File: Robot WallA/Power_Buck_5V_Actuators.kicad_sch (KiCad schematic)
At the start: 18 parts, among them J14 NID35-5, Q1 BSS138

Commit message: Continue to route
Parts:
- C57: footprint Capacitor_SMD:C_0805_2012Metric_Pad1.18x1.45mm_HandSolder -> SamacSys_Parts:EEE1AA220WR; Height (none) -> 5.5; Manufacturer_Part_Number (none) -> EEE-FN1E220R
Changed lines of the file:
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@@
+	)
+	(junction
+		(at 210.82 55.88)
+		(diameter 0)
+		(color 0 0 0 0)
+	)
+	(junction
+		(at 210.82 48.26)
+		(diameter 0)
+		(color 0 0 0 0)
 	)
 	(junction
@@
 	)
 	(junction
-		(at 209.55 55.88)
-		(diameter 0)
-		(color 0 0 0 0)
-	)
-	(junction
 		(at 138.43 80.01)
 		(diameter 0)
@@
 	)
 	(junction
-		(at 209.55 48.26)
-		(diameter 0)
-		(color 0 0 0 0)
-	)
-	(junction
 		(at 233.68 48.26)
 		(diameter 0)
@@
 	(wire
 		(pts
-			(xy 200.66 48.26) (xy 209.55 48.26)
+			(xy 200.66 48.26) (xy 210.82 48.26)
 		)
 		(stroke
@@
 	(wire
 		(pts
+			(xy 210.82 48.26) (xy 223.52 48.26)
+		)
+		(stroke
+			(width 0)
+			(type default)
+		)
+	)
+	(wire
+		(pts
+			(xy 210.82 55.88) (xy 223.52 55.88)
+		)
+		(stroke
+			(width 0)
+			(type default)
+		)
+	)
+	(wire
+		(pts
 			(xy 223.52 109.22) (xy 223.52 111.76)
 		)
@@
 	(wire
 		(pts
-			(xy 200.66 55.88) (xy 209.55 55.88)
-		)
-		(stroke
-			(width 0)
-			(type default)
-		)
-	)
-	(wire
-		(pts
 			(xy 87.63 54.61) (xy 97.79 54.61)
 		)
@@
 	(wire
 		(pts
-			(xy 209.55 55.88) (xy 223.52 55.88)
+			(xy 200.66 55.88) (xy 210.82 55.88)
 		)
 		(stroke
@@
 		(pts
 			(xy 138.43 80.01) (xy 138.43 82.55)
-		)
-		(stroke
-			(width 0)
-			(type default)
-		)
-	)
-	(wire
-		(pts
-			(xy 209.55 48.26) (xy 223.52 48.26)
 		)
 		(stroke
@@
 				(path "/117fd49e-499d-4b54-b58c-f6b538ecca4a/d5f4dab0-e2de-4083-971d-4b1eb9c8d4bb/1e067d8d-e8a8-481d-ab40-c8016ce22eb0"
 					(reference "#FLG05")
-					(unit 1)
-				)
-			)
-		)
-	)
-	(symbol
-		(lib_id "Device:C_Polarized")
-		(at 209.55 52.07 0)
-		(unit 1)
-		(exclude_from_sim no)
-		(in_bom yes)
-		(on_board yes)
-		(dnp no)
-		(property "Reference" "C57"
-			(at 202.946 52.07 0)
-			(effects
-				(font
-					(size 1.27 1.27)
-				)
-				(justify left)
-			)
-		)
-		(property "Value" "22uF/25V"
-			(at 204.978 55.118 0)
-			(effects
-				(font
-					(size 1.27 1.27)
-				)
-				(justify left)
-			)
-		)
-		(property "Footprint" "Capacitor_SMD:C_0805_2012Metric_Pad1.18x1.45mm_HandSolder"
-			(at 210.5152 55.88 0)
-			(effects
-				(font
-					(size 1.27 1.27)
-				)
-				(hide yes)
-			)
-		)
-		(property "Datasheet" "~"
-			(at 209.55 52.07 0)
-			(effects
-				(font
-					(size 1.27 1.27)
-				)
-				(hide yes)
-			)
-		)
-		(property "Description" "Polarized capacitor"
-			(at 209.55 52.07 0)
-			(effects
-				(font
-					(size 1.27 1.27)
-				)
-				(hide yes)
-			)
-		)
-		(pin "1"
-		)
-		(pin "2"
-		)
-		(instances
-			(project "PCB"
-				(path "/117fd49e-499d-4b54-b58c-f6b538ecca4a/d5f4dab0-e2de-4083-971d-4b1eb9c8d4bb/1e067d8d-e8a8-481d-ab40-c8016ce22eb0"
-					(reference "C57")
 					(unit 1)
 				)
@@
 					(unit 1)
 				)
+			)
+		)
+	)
+	(symbol
+		(lib_id "Device:C_Polarized")
+		(at 210.82 52.07 0)
+		(unit 1)
+		(exclude_from_sim no)
+		(in_bom yes)
+		(on_board yes)
+		(dnp no)
+		(property "Reference" "C57"
+			(at 204.216 52.07 0)
+			(effects
+				(font
+					(size 1.27 1.27)
+				)
+				(justify left)
+			)
+		)
+		(property "Value" "22uF/25V"
+			(at 206.248 55.118 0)
+			(effects
+				(font
+					(size 1.27 1.27)
+				)
+				(justify left)
+			)
+		)
+		(property "Footprint" "SamacSys_Parts:EEE1AA220WR"
+			(at 211.7852 55.88 0)
+			(effects
+				(font
+					(size 1.27 1.27)
+				)
+				(hide yes)
+			)
+		)
+		(property "Datasheet" "~"
+			(at 210.82 52.07 0)
+			(effects
+				(font
+					(size 1.27 1.27)
+				)
+				(hide yes)
+			)
+		)
+		(property "Description" "Polarized capacitor"
+			(at 210.82 52.07 0)
+			(effects
+				(font
+					(size 1.27 1.27)
+				)
+				(hide yes)
+			)
+		)
+		(property "Height" "5.5"
+			(at 210.82 52.07 0)
+			(effects
+				(font
+					(size 1.27 1.27)
+				)
+				(hide yes)
+			)
+		)
+		(property "Manufacturer_Part_Number" "EEE-FN1E220R"
+			(at 210.82 52.07 0)
+			(effects
+				(font
+					(size 1.27 1.27)
+				)
+				(hide yes)
+			)
+		)
+		(pin "1"
+		)
+		(pin "2"
+		)
+		(instances
+			(project "Robot WallA"
+				(path "/117fd49e-499d-4b54-b58c-f6b538ecca4a/d5f4dab0-e2de-4083-971d-4b1eb9c8d4bb/1e067d8d-e8a8-481d-ab40-c8016ce22eb0"
+					(reference "C57")
+					(unit 1)
+				)

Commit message: Reworked 12V and 5V power supplies, continue routing
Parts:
- removed C51: 120uF/25V, SamacSys_Parts:EEE0JA331XP, symbol Device:C_Polarized
- removed C52, C53, C54: 47nF/25V, Capacitor_SMD:C_0603_1608Metric_Pad1.08x0.95mm_HandSolder, symbol Device:C
- removed C55, C56: 4.7uF/25V, Capacitor_SMD:C_1210_3225Metric_Pad1.33x2.70mm_HandSolder, symbol Device:C
- removed C57: 22uF/25V, SamacSys_Parts:EEE1AA220WR, symbol Device:C_Polarized
- removed C58, C59, C60: 4.7uF/50V, Capacitor_SMD:C_0805_2012Metric_Pad1.18x1.45mm_HandSolder, symbol Device:C
- removed C61: 10nF/50V, Capacitor_SMD:C_0805_2012Metric_Pad1.18x1.45mm_HandSolder, symbol Device:C
- removed J14: NID35-5, SamacSys_Parts:NID355, symbol SamacSys_Parts:NID35-5
- removed Q1: BSS138, Package_TO_SOT_SMD:SOT-23, symbol Transistor_FET:BSS138
- removed R31: 100k, Resistor_SMD:R_0603_1608Metric_Pad0.98x0.95mm_HandSolder, symbol Device:R
- removed R32: 10k, Resistor_SMD:R_0603_1608Metric_Pad0.98x0.95mm_HandSolder, symbol Device:R
- removed RV2: Trim 10k, SamacSys_Parts:TC33X2503E, symbol Device:R_Potentiometer_Trim
- added C118, C87: 4.7uF/50V, Capacitor_SMD:C_1210_3225Metric_Pad1.33x2.70mm_HandSolder, symbol Device:C
- added C119: 10nF/50V, Capacitor_SMD:C_0805_2012Metric_Pad1.18x1.45mm_HandSolder, symbol Device:C
- added C120: 2.2uF/50V, Capacitor_SMD:C_1210_3225Metric_Pad1.33x2.70mm_HandSolder, symbol Device:C
- added C121, C122, C123: 47nF/25V, Capacitor_SMD:C_0603_1608Metric_Pad1.08x0.95mm_HandSolder, symbol Device:C
- added C124, C125: 4.7uF/25V, Capacitor_SMD:C_1210_3225Metric_Pad1.33x2.70mm_HandSolder, symbol Device:C
- added C86: 330uF, SamacSys_Parts:CAPPRD500W65D1000H1800, symbol Device:C_Polarized
- added JP12: Closed, Jumper:SolderJumper-2_P1.3mm_Bridged_RoundedPad1.0x1.5mm, symbol Jumper:Jumper_2_Bridged
- added JP13: Open, Jumper:SolderJumper-2_P1.3mm_Open_RoundedPad1.0x1.5mm, symbol Jumper:Jumper_2_Open
- added Q6: BSS138, Package_TO_SOT_SMD:SOT-23, symbol Transistor_FET:BSS138
- added R54: 21k, Resistor_SMD:R_0603_1608Metric_Pad0.98x0.95mm_HandSolder, symbol Device:R
- added R60: 10k, Resistor_SMD:R_0603_1608Metric_Pad0.98x0.95mm_HandSolder, symbol Device:R
- added RV3: Trim 2k, SamacSys_Parts:TC42X2202E, symbol Device:R_Potentiometer_Trim
- added U9: PTN78060W_EUW-7, Module:Texas_EUW_R-PDSS-T7_THT, symbol Converter_DCDC:PTN78060W_EUW-7
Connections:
- net GND: now also C118.2, C119.2, C120.2, C121.2, C122.2, C123.2, C124.2, C125.2, C86.2, C87.2, JP12.1 (A), Q6.2 (S), R60.2, RV3.2, U9.1 (GND), U9.7 (GND)
- net GPIO_ENABLE_5V: now also Q6.1 (G), R60.1
- net IN: now also C120.1, C121.1, C122.1, C123.1, C124.1, C125.1, U9.2 (VI)
- net OUT: now also C118.1, C119.1, C86.1, C87.1, U9.5 (VO_Sense), U9.6 (VO)
- new net: Q6.3 (D), U9.3 (~{Inhibit})
- new net: JP12.2 (B), JP13.1 (A), R54.2
- new net: JP13.2 (B), RV3.1
- new net TRIM: R54.1, U9.4 (VO_Adj)
- no-connect marks 0 -> 1
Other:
- note removed: "Si Vin=16V et Vout 5V --> Rendement >93% Avec un courant de 3A théorique (PC calcul) --> Puissance à dissiper de 1,05W Ne doit pas dépasser 55°C D'après la doc il ne faut pas forcément de radiateur, juste un ventilo Mettre un capteur de température pour monitorer?"
- note removed: "footprint size 10n --> 0805 47n --> 0603 4,7uF --> 1210"
- moved on the sheet: D5, R30

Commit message: Correct a lot of error in DRC
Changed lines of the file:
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@@
-	)
-	(junction
-		(at 261.62 29.21)
-		(diameter 0)
-		(color 0 0 0 0)
 	)
 	(junction
@@
 	(wire
 		(pts
-			(xy 257.81 29.21) (xy 261.62 29.21)
-		)
-		(stroke
-			(width 0)
-			(type default)
-		)
-	)
-	(wire
-		(pts
 			(xy 154.94 96.52) (xy 153.67 96.52)
 		)
@@
 	(wire
 		(pts
-			(xy 261.62 29.21) (xy 264.16 29.21)
+			(xy 257.81 29.21) (xy 264.16 29.21)
 		)
 		(stroke
@@
 	)
 	(symbol
+		(lib_id "power:PWR_FLAG")
+		(at 43.18 46.99 0)
+		(unit 1)
+		(exclude_from_sim no)
+		(in_bom yes)
+		(on_board yes)
+		(dnp no)
+		(fields_autoplaced yes)
+		(property "Reference" "#FLG07"
+			(at 43.18 45.085 0)
+			(effects
+				(font
+					(size 1.27 1.27)
+				)
+				(hide yes)
+			)
+		)
+		(property "Value" "PWR_FLAG"
+			(at 43.18 41.91 0)
+			(effects
+				(font
+					(size 1.27 1.27)
+				)
+				(hide yes)
+			)
+		)
+		(property "Footprint" ""
+			(at 43.18 46.99 0)
+			(effects
+				(font
+					(size 1.27 1.27)
+				)
+				(hide yes)
+			)
+		)
+		(property "Datasheet" "~"
+			(at 43.18 46.99 0)
+			(effects
+				(font
+					(size 1.27 1.27)
+				)
+				(hide yes)
+			)
+		)
+		(property "Description" "Special symbol for telling ERC where power comes from"
+			(at 43.18 46.99 0)
+			(effects
+				(font
+					(size 1.27 1.27)
+				)
+				(hide yes)
+			)
+		)
+		(pin "1"
+		)
+		(instances
+			(project "Robot WallA"
+				(path "/117fd49e-499d-4b54-b58c-f6b538ecca4a/d5f4dab0-e2de-4083-971d-4b1eb9c8d4bb/1e067d8d-e8a8-481d-ab40-c8016ce22eb0"
+					(reference "#FLG07")
+					(unit 1)
+				)
+			)
+		)
+	)
+	(symbol
 		(lib_id "Jumper:Jumper_2_Open")
 		(at 248.92 115.57 90)
@@
 					(unit 1)
 				)
-			)
-		)
-	)
-	(symbol
-		(lib_id "power:PWR_FLAG")
-		(at 261.62 29.21 0)
-		(unit 1)
-		(exclude_from_sim no)
-		(in_bom yes)
-		(on_board yes)
-		(dnp no)
-		(fields_autoplaced yes)
-		(property "Reference" "#FLG05"
-			(at 261.62 27.305 0)
-			(effects
-				(font
-					(size 1.27 1.27)
-				)
-				(hide yes)
-			)
-		)
-		(property "Value" "PWR_FLAG"
-			(at 261.62 24.13 0)
-			(effects
-				(font
-					(size 1.27 1.27)
-				)
-				(hide yes)
-			)
-		)
-		(property "Footprint" ""
-			(at 261.62 29.21 0)
-			(effects
-				(font
-					(size 1.27 1.27)
-				)
-				(hide yes)
-			)
-		)
-		(property "Datasheet" "~"
-			(at 261.62 29.21 0)
-			(effects
-				(font
-					(size 1.27 1.27)
-				)
-				(hide yes)
-			)
-		)
-		(property "Description" "Special symbol for telling ERC where power comes from"
-			(at 261.62 29.21 0)
-			(effects
-				(font
-					(size 1.27 1.27)
-				)
-				(hide yes)
-			)
-		)
-		(pin "1"
-		)
-		(instances
-			(project "Robot WallA"
-				(path "/117fd49e-499d-4b54-b58c-f6b538ecca4a/d5f4dab0-e2de-4083-971d-4b1eb9c8d4bb/1e067d8d-e8a8-481d-ab40-c8016ce22eb0"
-					(reference "#FLG05")
-					(unit 1)
-				)

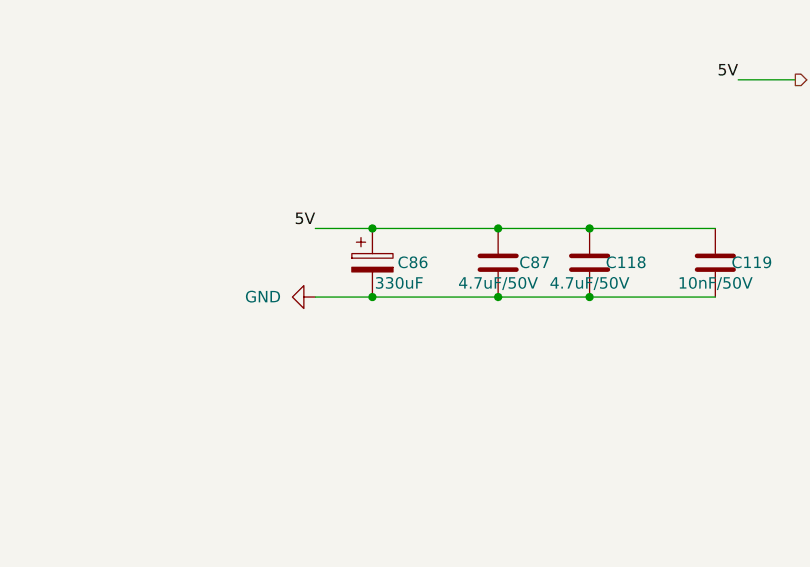
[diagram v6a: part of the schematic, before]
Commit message: Corrected all DRC erros, added info on PCB
modified distance meter connectors to be horizontal
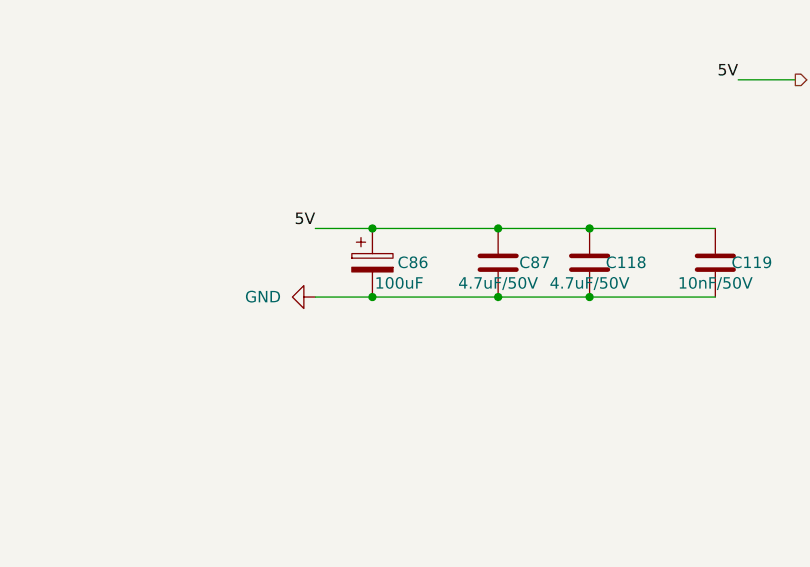
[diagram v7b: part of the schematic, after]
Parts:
- C86: value 330uF -> 100uF; footprint SamacSys_Parts:CAPPRD500W65D1000H1800 -> SamacSys_Parts:CAPPRD350W65D800H1250; Manufacturer_Part_Number EEU-FC1V331 -> (none)
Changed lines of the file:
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@@
+	)
+	(junction
+		(at 231.14 45.72)
+		(diameter 0)
+		(color 0 0 0 0)
+	)
+	(junction
+		(at 217.17 53.34)
+		(diameter 0)
+		(color 0 0 0 0)
+	)
+	(junction
+		(at 154.94 97.79)
+		(diameter 0)
+		(color 0 0 0 0)
+	)
+	(junction
+		(at 118.11 113.03)
+		(diameter 0)
+		(color 0 0 0 0)
+	)
+	(junction
+		(at 64.77 54.61)
+		(diameter 0)
+		(color 0 0 0 0)
+	)
+	(junction
+		(at 55.88 54.61)
+		(diameter 0)
+		(color 0 0 0 0)
+	)
+	(junction
+		(at 243.84 110.49)
+		(diameter 0)
+		(color 0 0 0 0)
+	)
+	(junction
+		(at 43.18 54.61)
+		(diameter 0)
+		(color 0 0 0 0)
+	)
+	(junction
+		(at 87.63 46.99)
+		(diameter 0)
+		(color 0 0 0 0)
+	)
+	(junction
+		(at 241.3 53.34)
+		(diameter 0)
+		(color 0 0 0 0)
+	)
+	(junction
+		(at 241.3 45.72)
+		(diameter 0)
+		(color 0 0 0 0)
+	)
+	(junction
+		(at 107.95 104.14)
+		(diameter 0)
+		(color 0 0 0 0)
+	)
+	(junction
+		(at 73.66 46.99)
+		(diameter 0)
+		(color 0 0 0 0)
+	)
+	(junction
+		(at 73.66 54.61)
+		(diameter 0)
+		(color 0 0 0 0)
+	)
+	(junction
+		(at 55.88 46.99)
+		(diameter 0)
+		(color 0 0 0 0)
+	)
+	(junction
+		(at 231.14 53.34)
+		(diameter 0)
+		(color 0 0 0 0)
+	)
+	(junction
+		(at 64.77 46.99)
+		(diameter 0)
+		(color 0 0 0 0)
 	)
 	(junction
@@
 	)
 	(junction
-		(at 231.14 45.72)
-		(diameter 0)
-		(color 0 0 0 0)
-	)
-	(junction
-		(at 154.94 97.79)
-		(diameter 0)
-		(color 0 0 0 0)
-	)
-	(junction
-		(at 118.11 113.03)
-		(diameter 0)
-		(color 0 0 0 0)
-	)
-	(junction
-		(at 64.77 54.61)
-		(diameter 0)
-		(color 0 0 0 0)
-	)
-	(junction
-		(at 55.88 54.61)
-		(diameter 0)
-		(color 0 0 0 0)
-	)
-	(junction
-		(at 243.84 110.49)
-		(diameter 0)
-		(color 0 0 0 0)
-	)
-	(junction
-		(at 43.18 54.61)
-		(diameter 0)
-		(color 0 0 0 0)
-	)
-	(junction
-		(at 87.63 46.99)
-		(diameter 0)
-		(color 0 0 0 0)
-	)
-	(junction
-		(at 241.3 53.34)
-		(diameter 0)
-		(color 0 0 0 0)
-	)
-	(junction
-		(at 241.3 45.72)
-		(diameter 0)
-		(color 0 0 0 0)
-	)
-	(junction
-		(at 107.95 104.14)
-		(diameter 0)
-		(color 0 0 0 0)
-	)
-	(junction
-		(at 73.66 46.99)
-		(diameter 0)
-		(color 0 0 0 0)
-	)
-	(junction
-		(at 217.17 53.34)
-		(diameter 0)
-		(color 0 0 0 0)
-	)
-	(junction
-		(at 73.66 54.61)
-		(diameter 0)
-		(color 0 0 0 0)
-	)
-	(junction
-		(at 55.88 46.99)
-		(diameter 0)
-		(color 0 0 0 0)
-	)
-	(junction
-		(at 231.14 53.34)
-		(diameter 0)
-		(color 0 0 0 0)
-	)
-	(junction
-		(at 64.77 46.99)
-		(diameter 0)
-		(color 0 0 0 0)
-	)
-	(junction
 		(at 87.63 54.61)
 		(diameter 0)
@@
 	(wire
 		(pts
+			(xy 210.82 45.72) (xy 217.17 45.72)
+		)
+		(stroke
+			(width 0)
+			(type default)
+		)
+	)
+	(wire
+		(pts
+			(xy 241.3 45.72) (xy 255.27 45.72)
+		)
+		(stroke
+			(width 0)
+			(type default)
+		)
+	)
+	(wire
+		(pts
 			(xy 217.17 45.72) (xy 231.14 45.72)
 		)
@@
 	(wire
 		(pts
-			(xy 241.3 45.72) (xy 255.27 45.72)
-		)
-		(stroke
-			(width 0)
-			(type default)
-		)
-	)
-	(wire
-		(pts
-			(xy 210.82 45.72) (xy 217.17 45.72)
-		)
-		(stroke
-			(width 0)
-			(type default)
-		)
-	)
-	(wire
-		(pts
 			(xy 55.88 54.61) (xy 64.77 54.61)
 		)
@@
 	(wire
 		(pts
+			(xy 217.17 53.34) (xy 231.14 53.34)
+		)
+		(stroke
+			(width 0)
+			(type default)
+		)
+	)
+	(wire
+		(pts
 			(xy 43.18 54.61) (xy 55.88 54.61)
 		)
@@
 		(pts
 			(xy 87.63 54.61) (xy 97.79 54.61)
-		)
-		(stroke
-			(width 0)
-			(type default)
-		)
-	)
-	(wire
-		(pts
-			(xy 217.17 53.34) (xy 231.14 53.34)
 		)
 		(stroke
@@
 	)
 	(symbol
+		(lib_id "Device:C_Polarized")
+		(at 217.17 49.53 0)
+		(unit 1)
+		(exclude_from_sim no)
+		(in_bom yes)
+		(on_board yes)
+		(dnp no)
+		(property "Reference" "C86"
+			(at 219.964 49.53 0)
+			(effects
+				(font
+					(size 1.27 1.27)
+				)
+				(justify left)
+			)
+		)
+		(property "Value" "100uF"
+			(at 217.424 51.816 0)
+			(effects
+				(font
+					(size 1.27 1.27)
+				)
+				(justify left)
+			)
+		)
+		(property "Footprint" "SamacSys_Parts:CAPPRD350W65D800H1250"
+			(at 218.1352 53.34 0)
+			(effects
+				(font
+					(size 1.27 1.27)
+				)
+				(hide yes)
+			)
+		)
+		(property "Datasheet" "~"
+			(at 217.17 49.53 0)
+			(effects
+				(font
+					(size 1.27 1.27)
+				)
+				(hide yes)
+			)
+		)
+		(property "Description" "Polarized capacitor"
+			(at 217.17 49.53 0)
+			(effects
+				(font
+					(size 1.27 1.27)
+				)
+				(hide yes)
+			)
+		)
+		(property "Manufacturer_Part_Number" ""
+			(at 217.17 49.53 0)
+			(effects
+				(font
+					(size 1.27 1.27)
+				)
+				(hide yes)
+			)
+		)
+		(pin "1"
+		)
+		(pin "2"
+		)
+		(instances
+			(project "Robot WallA"
+				(path "/117fd49e-499d-4b54-b58c-f6b538ecca4a/d5f4dab0-e2de-4083-971d-4b1eb9c8d4bb/1e067d8d-e8a8-481d-ab40-c8016ce22eb0"
+					(reference "C86")
+					(unit 1)
+				)
+			)
+		)
+	)
+	(symbol
 		(lib_id "Device:C")
 		(at 231.14 49.53 0)
@@
 					(unit 1)
 				)
-			)
-		)
-	)
-	(symbol
-		(lib_id "Device:C_Polarized")
-		(at 217.17 49.53 0)
-		(unit 1)
-		(exclude_from_sim no)
-		(in_bom yes)
-		(on_board yes)
-		(dnp no)
-		(property "Reference" "C86"
-			(at 219.964 49.53 0)
-			(effects
-				(font
-					(size 1.27 1.27)
-				)
-				(justify left)
-			)
-		)
-		(property "Value" "330uF"
-			(at 217.424 51.816 0)
-			(effects
-				(font
-					(size 1.27 1.27)
-				)
-				(justify left)
-			)
-		)
-		(property "Footprint" "SamacSys_Parts:CAPPRD500W65D1000H1800"
-			(at 218.1352 53.34 0)
-			(effects
-				(font
-					(size 1.27 1.27)
-				)
-				(hide yes)
-			)
-		)
-		(property "Datasheet" "~"
-			(at 217.17 49.53 0)
-			(effects
-				(font
-					(size 1.27 1.27)
-				)
-				(hide yes)
-			)
-		)
-		(property "Description" "Polarized capacitor"
-			(at 217.17 49.53 0)
-			(effects
-				(font
-					(size 1.27 1.27)
-				)
-				(hide yes)
-			)
-		)
-		(property "Manufacturer_Part_Number" "EEU-FC1V331"
-			(at 217.17 49.53 0)
-			(effects
-				(font
-					(size 1.27 1.27)
-				)
-				(hide yes)
-			)
-		)
-		(pin "1"
-		)
-		(pin "2"
-		)
-		(instances
-			(project "Robot WallA"
-				(path "/117fd49e-499d-4b54-b58c-f6b538ecca4a/d5f4dab0-e2de-4083-971d-4b1eb9c8d4bb/1e067d8d-e8a8-481d-ab40-c8016ce22eb0"
-					(reference "C86")
-					(unit 1)
-				)

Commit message: Updated fab files.
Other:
- company: (none) -> Socotec Monitoring
- title: (none) -> Robot Wall-A
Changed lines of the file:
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@@
 	(generator_version "9.0")
 	(paper "A4")
+	(title_block
+		(title "Robot Wall-A")
+		(date "2025-09-20")
+		(rev "v1.0")
+		(company "Socotec Monitoring")
+		(comment 1 "GDU")
+		(comment 2 "THO")
+	)
 	(junction
 		(at 43.18 46.99)
@@
 			)
 		)
+		(property "MPN" ""
+			(at 55.88 50.8 0)
+			(effects
+				(font
+					(size 1.27 1.27)
+				)
+				(hide yes)
+			)
+		)
 		(pin "1"
 		)
@@
 			)
 		)
+		(property "MPN" ""
+			(at 115.57 104.14 0)
+			(effects
+				(font
+					(size 1.27 1.27)
+				)
+				(hide yes)
+			)
+		)
 		(pin "2"
 		)
@@
 			)
 		)
+		(property "MPN" ""
+			(at 87.63 50.8 0)
+			(effects
+				(font
+					(size 1.27 1.27)
+				)
+				(hide yes)
+			)
+		)
 		(pin "1"
 		)
@@
 			)
 		)
+		(property "MPN" ""
+			(at 107.95 109.22 90)
+			(effects
+				(font
+					(size 1.27 1.27)
+				)
+				(hide yes)
+			)
+		)
 		(pin "1"
 		)
@@
 			)
 		)
+		(property "MPN" ""
+			(at 248.92 115.57 90)
+			(effects
+				(font
+					(size 1.27 1.27)
+				)
+				(hide yes)
+			)
+		)
 		(pin "1"
 		)
@@
 			)
 		)
+		(property "MPN" ""
+			(at 64.77 50.8 0)
+			(effects
+				(font
+					(size 1.27 1.27)
+				)
+				(hide yes)
+			)
+		)
 		(pin "1"
 		)
@@
 			)
 		)
+		(property "MPN" ""
+			(at 157.48 50.8 90)
+			(effects
+				(font
+					(size 1.27 1.27)
+				)
+				(hide yes)
+			)
+		)
 		(pin "1"
 		)
@@
 			)
 		)
+		(property "MPN" ""
+			(at 238.76 115.57 90)
+			(effects
+				(font
+					(size 1.27 1.27)
+				)
+				(hide yes)
+			)
+		)
 		(pin "2"
 		)
@@
 			)
 		)
+		(property "MPN" ""
+			(at 255.27 49.53 0)
+			(effects
+				(font
+					(size 1.27 1.27)
+				)
+				(hide yes)
+			)
+		)
 		(pin "1"
 		)
@@
 			)
 		)
+		(property "MPN" ""
+			(at 248.92 124.46 0)
+			(effects
+				(font
+					(size 1.27 1.27)
+				)
+				(hide yes)
+			)
+		)
 		(pin "2"
 		)
@@
 			)
 		)
+		(property "MPN" ""
+			(at 97.79 50.8 0)
+			(effects
+				(font
+					(size 1.27 1.27)
+				)
+				(hide yes)
+			)
+		)
 		(pin "1"
 		)
@@
 			)
 		)
+		(property "MPN" ""
+			(at 140.97 99.06 0)
+			(effects
+				(font
+					(size 1.27 1.27)
+				)
+				(hide yes)
+			)
+		)
 		(pin "4"
 		)
@@
 			)
 		)
+		(property "MPN" ""
+			(at 43.18 50.8 0)
+			(effects
+				(font
+					(size 1.27 1.27)
+				)
+				(hide yes)
+			)
+		)
 		(pin "1"
 		)
@@
 			)
 		)
+		(property "MPN" ""
+			(at 147.32 50.8 0)
+			(effects
+				(font
+					(size 1.27 1.27)
+				)
+				(hide yes)
+			)
+		)
 		(pin "2"
 		)
@@
 			)
 		)
+		(property "MPN" ""
+			(at 217.17 49.53 0)
+			(effects
+				(font
+					(size 1.27 1.27)
+				)
+				(hide yes)
+			)
+		)
 		(pin "1"
 		)
@@
 			)
 		)
+		(property "MPN" ""
+			(at 231.14 49.53 0)
+			(effects
+				(font
+					(size 1.27 1.27)
+				)
+				(hide yes)
+			)
+		)
 		(pin "1"
 		)
@@
 			)
 		)
+		(property "MPN" ""
+			(at 243.84 106.68 0)
+			(effects
+				(font
+					(size 1.27 1.27)
+				)
+				(hide yes)
+			)
+		)
 		(pin "1"
 		)
@@
 			)
 		)
+		(property "MPN" ""
+			(at 241.3 49.53 0)
+			(effects
+				(font
+					(size 1.27 1.27)
+				)
+				(hide yes)
+			)
+		)
 		(pin "1"
 		)
@@
 			(at 73.66 50.8 0)
 			(effects
+				(font
+					(size 1.27 1.27)
+				)
+				(hide yes)
+			)
+		)
+		(property "MPN" ""
+			(at 73.66 50.8 0)
+			(effects
